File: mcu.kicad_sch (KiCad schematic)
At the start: 11 parts

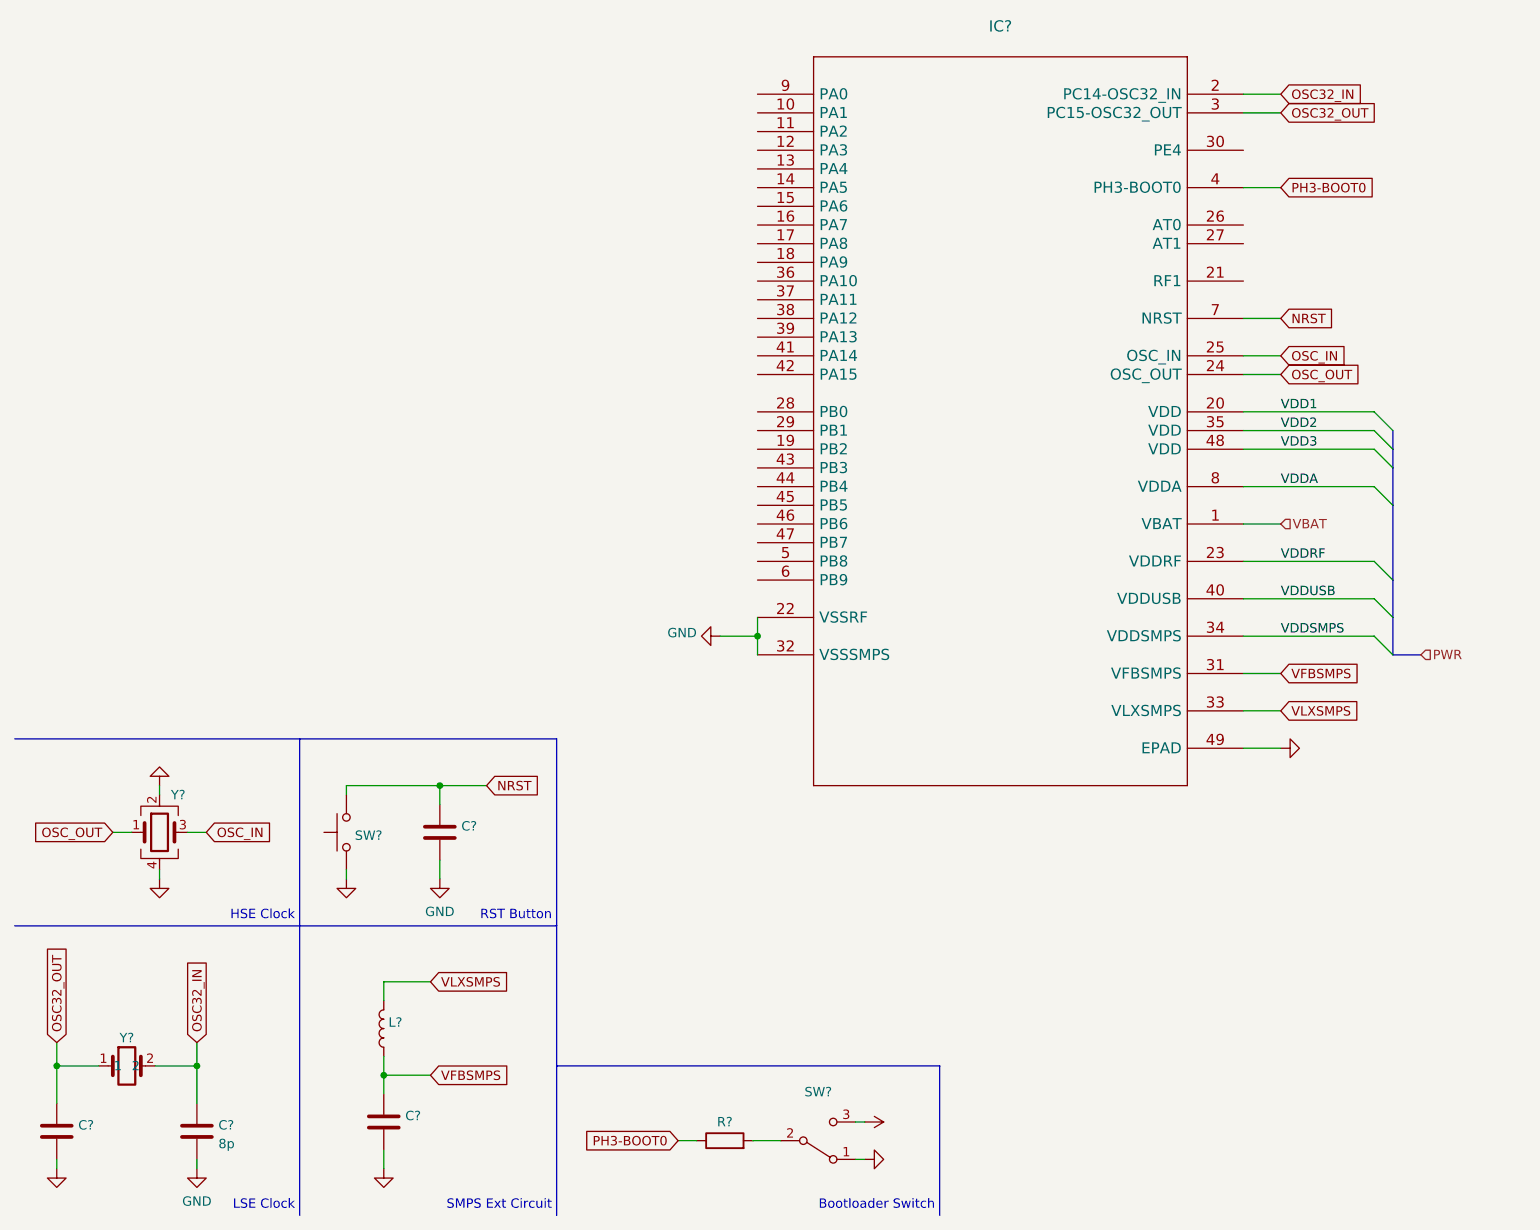
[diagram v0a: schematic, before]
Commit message: Added connectors
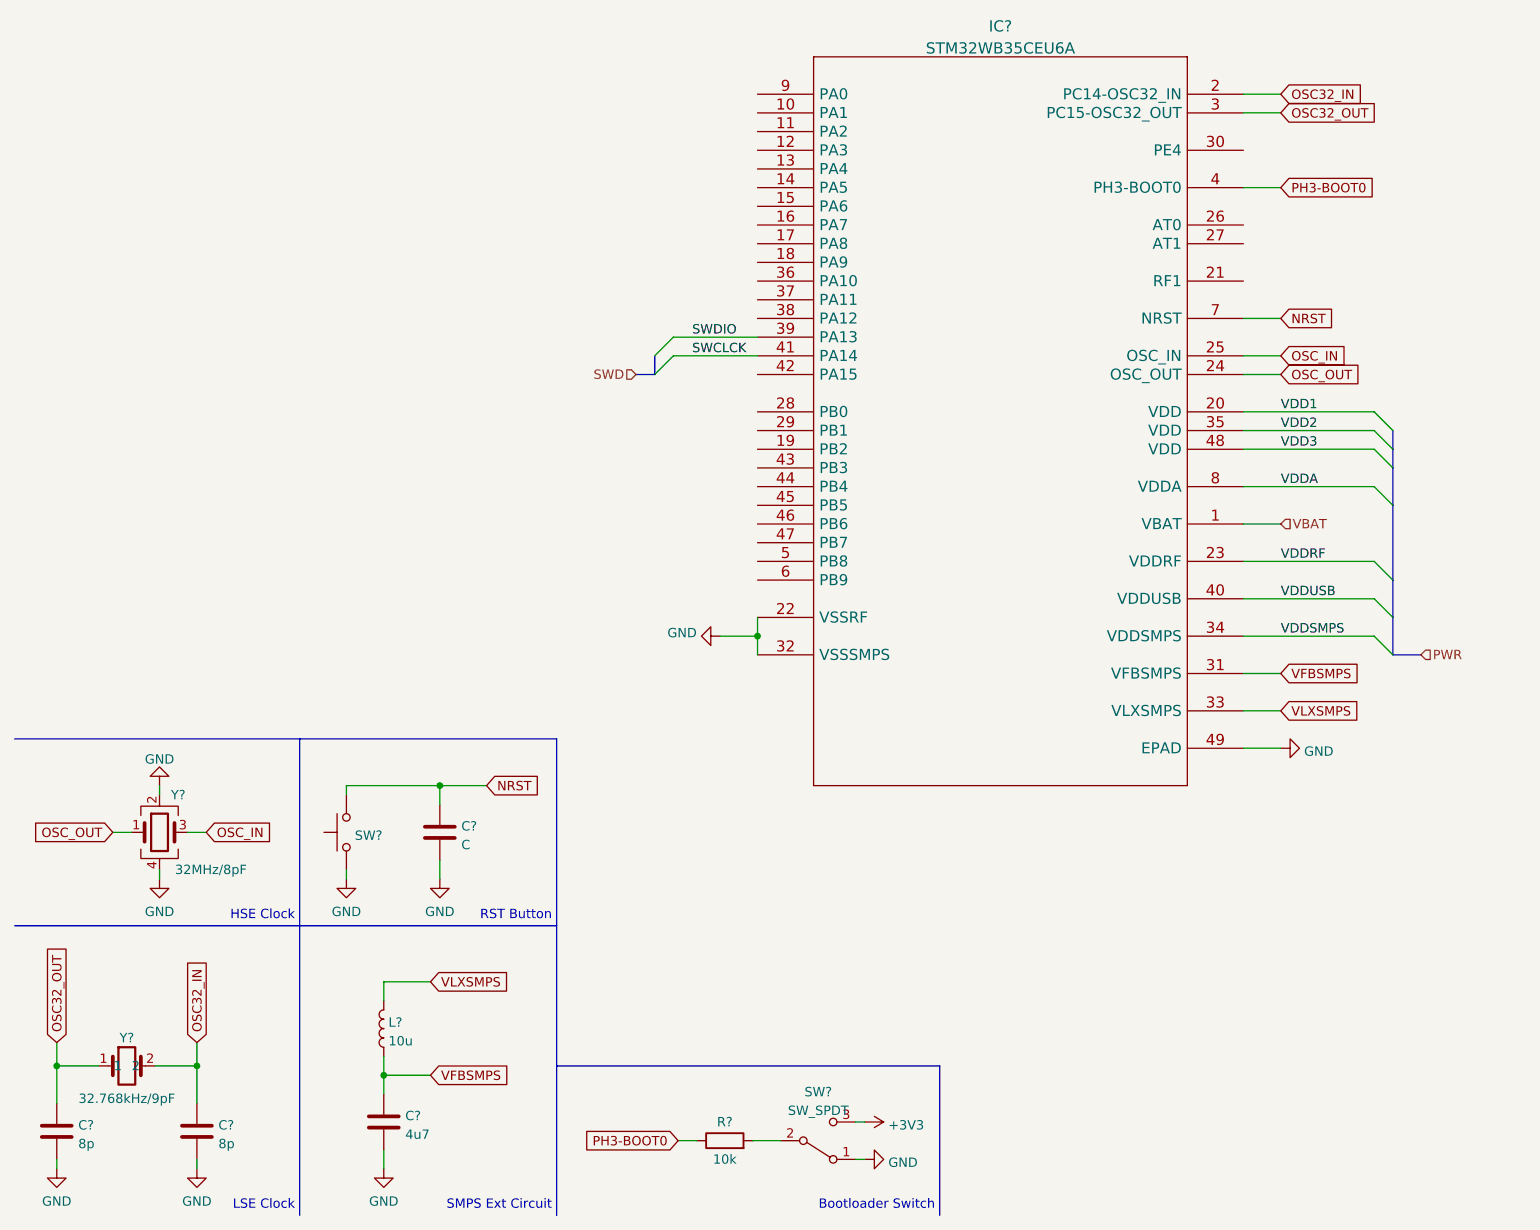
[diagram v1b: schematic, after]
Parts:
- C?: value (none) -> 8p
- C?: value (none) -> C
- C?: value (none) -> 4u7
- IC?: value (none) -> STM32WB35CEU6A; footprint (none) -> OxySwitch:STM32WB35CEU6A
- L?: value (none) -> 10u
- R?: value (none) -> 10k
- SW?: value (none) -> SW_Push
- SW?: value (none) -> SW_SPDT
- Y?: value (none) -> 32.768kHz/9pF; footprint (none) -> ABS0532768KHZ9T
- Y?: value (none) -> 32MHz/8pF; footprint (none) -> ABM11W300000MHZ4B1UT3
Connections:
- net SWDIO: now reaches IC?.39 (PA13)
- net SWCLCK: now reaches IC?.41 (PA14)
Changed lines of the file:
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@@
+    (stroke (width 0) (type default) (color 0 0 0 0))
+  )
+  (bus_entry (at 99.06 83.82) (size 2.54 -2.54)
+    (stroke (width 0) (type default) (color 0 0 0 0))
+  )
+  (bus_entry (at 99.06 81.28) (size 2.54 -2.54)
     (stroke (width 0) (type default) (color 0 0 0 0))
   )
@@
     (stroke (width 0) (type default) (color 0 0 0 0))
   )
+  (bus (pts (xy 99.06 83.82) (xy 96.52 83.82))
+    (stroke (width 0) (type default) (color 0 0 0 0))
+  )
   (bus (pts (xy 199.39 93.98) (xy 199.39 96.52))
     (stroke (width 0) (type default) (color 0 0 0 0))
@@
     (stroke (width 0) (type default) (color 0 0 0 0))
   )
+  (wire (pts (xy 101.6 81.28) (xy 113.03 81.28))
+    (stroke (width 0) (type default) (color 0 0 0 0))
+  )
   (wire (pts (xy 62.23 179.07) (xy 68.58 179.07))
     (stroke (width 0) (type default) (color 0 0 0 0))
@@
     (stroke (width 0) (type default) (color 0 0 0 0))
   )
+  (bus (pts (xy 99.06 81.28) (xy 99.06 83.82))
+    (stroke (width 0) (type default) (color 0 0 0 0))
+  )
   (wire (pts (xy 179.07 104.14) (xy 184.15 104.14))
     (stroke (width 0) (type default) (color 0 0 0 0))
@@
   )
   (wire (pts (xy 179.07 45.72) (xy 184.15 45.72))
+    (stroke (width 0) (type default) (color 0 0 0 0))
+  )
+  (wire (pts (xy 101.6 78.74) (xy 113.03 78.74))
     (stroke (width 0) (type default) (color 0 0 0 0))
   )
@@
   )
   (label "VDDA" (at 184.15 99.06 0)
+    (effects (font (size 1.27 1.27)) (justify left bottom))
+  )
+  (label "SWDIO" (at 104.14 78.74 0)
+    (effects (font (size 1.27 1.27)) (justify left bottom))
+  )
+  (label "SWCLCK" (at 104.14 81.28 0)
     (effects (font (size 1.27 1.27)) (justify left bottom))
   )
@@
     (effects (font (size 1.27 1.27)) (justify left))
   )
+  (hierarchical_label "SWD" (shape input) (at 96.52 83.82 180)
+    (effects (font (size 1.27 1.27)) (justify right))
+  )
   (symbol (lib_id "Device:C") (at 17.78 186.69 0) (unit 1)
     (in_bom yes) (on_board yes) (fields_autoplaced)
@@
       (effects (font (size 1.27 1.27)) (justify left))
     )
-    (property "Value" "" (id 1) (at 20.701 188.3922 0)
+    (property "Value" "8p" (id 1) (at 20.701 188.3922 0)
       (effects (font (size 1.27 1.27)) (justify left))
     )
@@
       (effects (font (size 1.27 1.27)) hide)
     )
-    (property "Value" "" (id 1) (at 62.23 196.2134 0))
+    (property "Value" "GND" (id 1) (at 62.23 196.2134 0))
     (property "Footprint" "" (id 2) (at 62.23 191.77 0)
       (effects (font (size 1.27 1.27)) hide)
@@
       (effects (font (size 1.27 1.27)) (justify left))
     )
-    (property "Value" "" (id 1) (at 72.771 147.7522 0)
+    (property "Value" "C" (id 1) (at 72.771 147.7522 0)
       (effects (font (size 1.27 1.27)) (justify left))
     )
@@
       (effects (font (size 1.27 1.27)) (justify right))
     )
-    (property "Value" "" (id 1) (at 58.293 147.7522 90)
+    (property "Value" "SW_Push" (id 1) (at 58.293 147.7522 90)
       (effects (font (size 1.27 1.27)) (justify right) hide)
     )
@@
       (effects (font (size 1.27 1.27)) hide)
     )
-    (property "Value" "" (id 1) (at 130.81 190.9338 90)
+    (property "Value" "GND" (id 1) (at 130.81 190.9338 90)
       (effects (font (size 1.27 1.27)) (justify right))
     )
@@
       (effects (font (size 1.27 1.27)) (justify right))
     )
-    (property "Value" "" (id 1) (at 62.865 174.4222 0)
+    (property "Value" "10u" (id 1) (at 62.865 174.4222 0)
       (effects (font (size 1.27 1.27)) (justify right))
     )
@@
       (effects (font (size 1.27 1.27)) hide)
     )
-    (property "Value" "" (id 1) (at 130.81 185.8538 90)
+    (property "Value" "+3V3" (id 1) (at 130.81 185.8538 90)
       (effects (font (size 1.27 1.27)) (justify left))
     )
@@
       (effects (font (size 1.524 1.524)))
     )
-    (property "Value" "" (id 1) (at 146.05 39.4858 0)
+    (property "Value" "STM32WB35CEU6A" (id 1) (at 146.05 39.4858 0)
       (effects (font (size 1.524 1.524)))
     )
-    (property "Footprint" "" (id 2) (at 146.05 39.624 0)
+    (property "Footprint" "OxySwitch:STM32WB35CEU6A" (id 2) (at 146.05 39.624 0)
       (effects (font (size 1.524 1.524)) hide)
     )
@@
       (effects (font (size 1.27 1.27)) hide)
     )
-    (property "Value" "" (id 1) (at 17.78 196.2134 0))
+    (property "Value" "GND" (id 1) (at 17.78 196.2134 0))
     (property "Footprint" "" (id 2) (at 17.78 191.77 0)
       (effects (font (size 1.27 1.27)) hide)
@@
     (in_bom yes) (on_board yes)
     (property "Reference" "R?" (id 0) (at 108.585 185.42 90))
-    (property "Value" "" (id 1) (at 108.585 190.5 90))
+    (property "Value" "10k" (id 1) (at 108.585 190.5 90))
     (property "Footprint" "" (id 2) (at 108.585 189.738 90)
       (effects (font (size 1.27 1.27)) hide)
@@
     (in_bom yes) (on_board yes)
     (property "Reference" "Y?" (id 0) (at 27.305 173.99 0))
-    (property "Value" "" (id 1) (at 27.305 182.245 0))
-    (property "Footprint" "" (id 2) (at 36.195 176.53 0)
+    (property "Value" "32.768kHz/9pF" (id 1) (at 27.305 182.245 0))
+    (property "Footprint" "ABS0532768KHZ9T" (id 2) (at 36.195 176.53 0)
       (effects (font (size 1.27 1.27)) (justify left) hide)
     )
@@
       (effects (font (size 1.27 1.27)) hide)
     )
-    (property "Value" "" (id 1) (at 57.15 156.8434 0))
+    (property "Value" "GND" (id 1) (at 57.15 156.8434 0))
     (property "Footprint" "" (id 2) (at 57.15 152.4 0)
       (effects (font (size 1.27 1.27)) hide)
@@
       (effects (font (size 1.27 1.27)) hide)
     )
-    (property "Value" "" (id 1) (at 31.75 156.8434 0))
+    (property "Value" "GND" (id 1) (at 31.75 156.8434 0))
     (property "Footprint" "" (id 2) (at 31.75 152.4 0)
       (effects (font (size 1.27 1.27)) hide)
@@
     (in_bom yes) (on_board yes) (fields_autoplaced)
     (property "Reference" "SW?" (id 0) (at 121.285 181.3392 0))
-    (property "Value" "" (id 1) (at 121.285 183.8761 0))
+    (property "Value" "SW_SPDT" (id 1) (at 121.285 183.8761 0))
     (property "Footprint" "" (id 2) (at 121.285 187.96 0)
       (effects (font (size 1.27 1.27)) hide)
@@
     (in_bom yes) (on_board yes)
     (property "Reference" "Y?" (id 0) (at 34.29 140.97 0))
-    (property "Value" "" (id 1) (at 38.735 151.13 0))
-    (property "Footprint" "" (id 2) (at 68.58 143.51 0)
+    (property "Value" "32MHz/8pF" (id 1) (at 38.735 151.13 0))
+    (property "Footprint" "ABM11W300000MHZ4B1UT3" (id 2) (at 68.58 143.51 0)
       (effects (font (size 1.27 1.27)) (justify left) hide)
     )
@@
       (effects (font (size 1.27 1.27)) hide)
     )
-    (property "Value" "" (id 1) (at 31.75 136.1242 0))
+    (property "Value" "GND" (id 1) (at 31.75 136.1242 0))
     (property "Footprint" "" (id 2) (at 31.75 139.7 0)
       (effects (font (size 1.27 1.27)) hide)
@@
       (effects (font (size 1.27 1.27)) (justify left))
     )
-    (property "Value" "" (id 1) (at 65.151 187.1222 0)
+    (property "Value" "4u7" (id 1) (at 65.151 187.1222 0)
       (effects (font (size 1.27 1.27)) (justify left))
     )
@@
       (effects (font (size 1.27 1.27)) hide)
     )
-    (property "Value" "" (id 1) (at 187.325 135.0538 90)
+    (property "Value" "GND" (id 1) (at 187.325 135.0538 90)
       (effects (font (size 1.27 1.27)) (justify right))
     )

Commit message: Added RF
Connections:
- net RF1: now reaches IC?.21 (RF1)
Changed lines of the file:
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@@
+    (stroke (width 0) (type default) (color 0 0 0 0))
+  )
+  (wire (pts (xy 179.07 71.12) (xy 184.15 71.12))
     (stroke (width 0) (type default) (color 0 0 0 0))
   )
@@
     (effects (font (size 1.27 1.27)) (justify right))
   )
+  (hierarchical_label "RF1" (shape input) (at 184.15 71.12 0)
+    (effects (font (size 1.27 1.27)) (justify left))
+  )
   (symbol (lib_id "Device:C") (at 17.78 186.69 0) (unit 1)
